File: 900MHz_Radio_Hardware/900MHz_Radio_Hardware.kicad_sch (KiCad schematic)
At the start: 27 parts, among them SW1 SW_SPDT, U1 TSR_1-2450

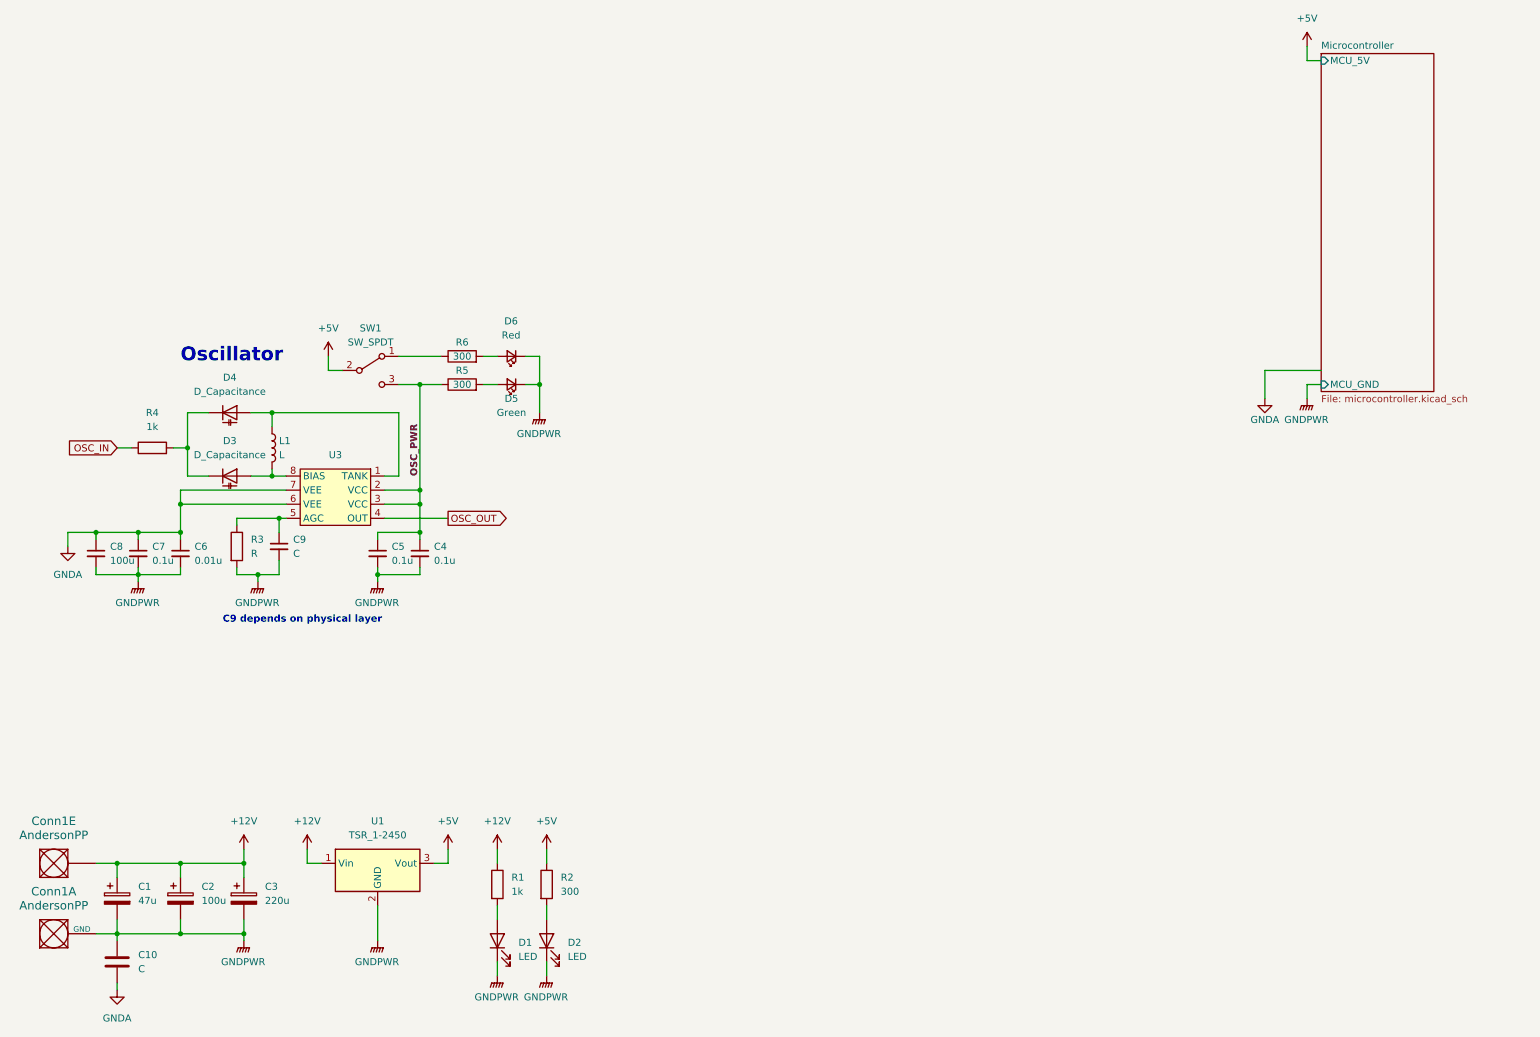
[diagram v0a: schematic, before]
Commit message: Worked on oscillator tank
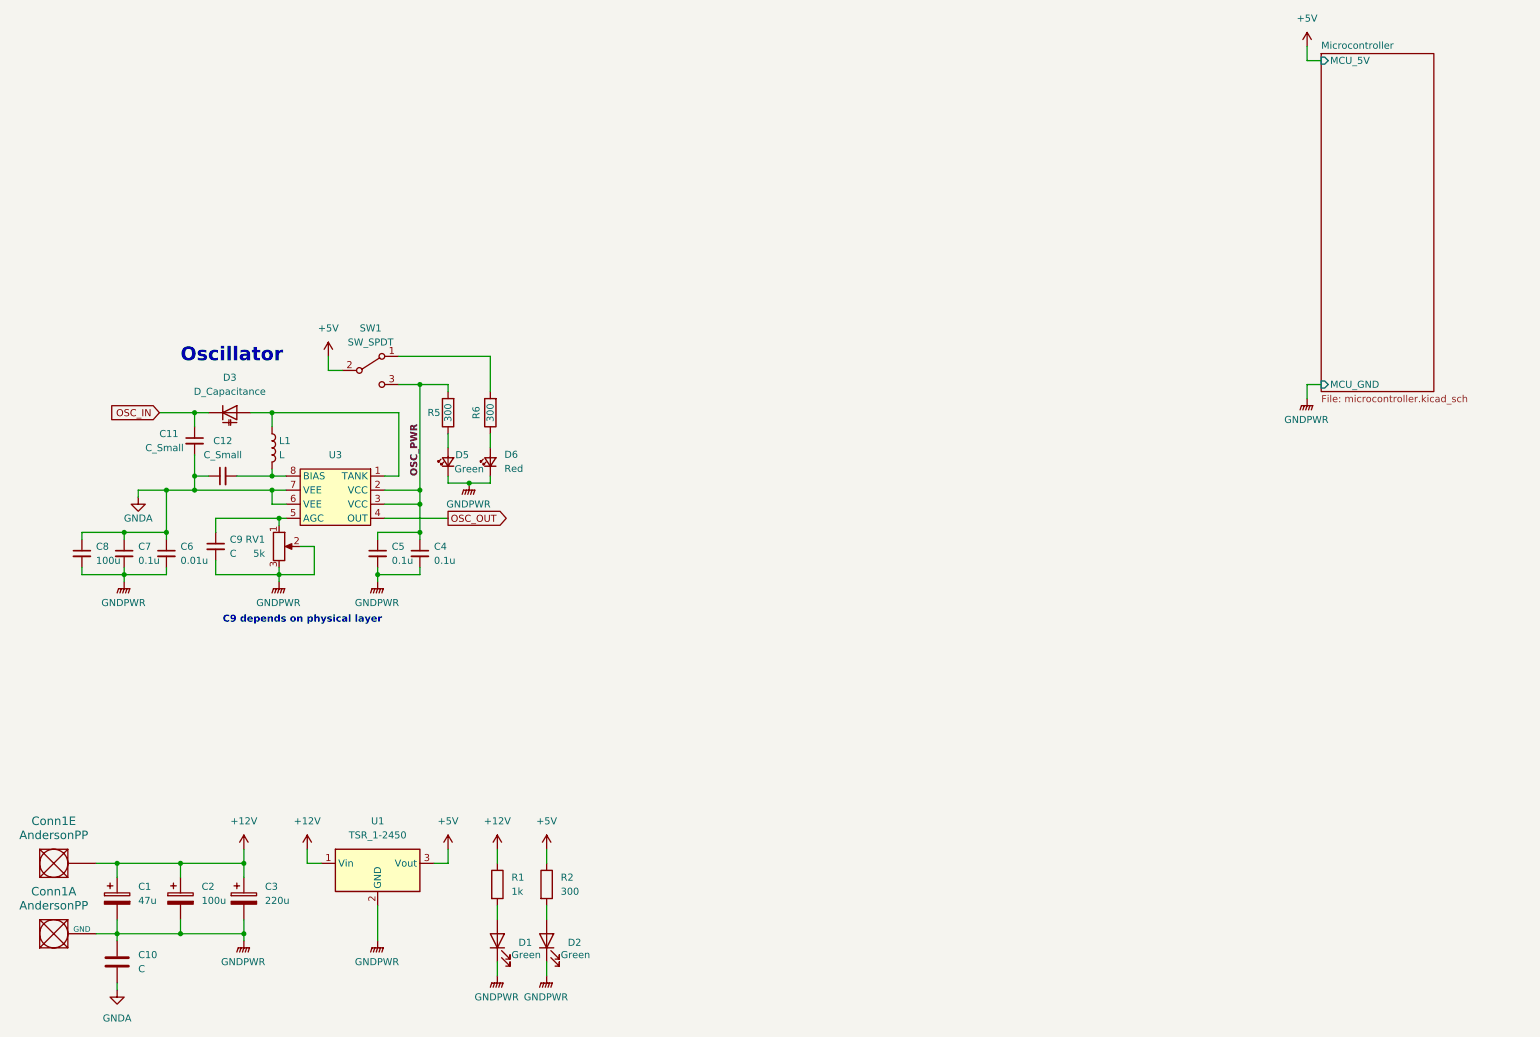
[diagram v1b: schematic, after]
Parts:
- removed D4: D_Capacitance, symbol Device:D_Capacitance
- removed R3: R, symbol Device:R
- removed R4: 1k, symbol Device:R
- added C11, C12: C_Small, symbol Device:C_Small
- added RV1: 5k, symbol Device:R_Potentiometer
- D1, D2: value LED -> Green
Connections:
- net GNDA: now also C11.2, C12.1
- net GNDPWR: now also RV1.2, RV1.3
- net OSC_IN: now also D3.1 (K), C11.1
- net OSC_PWR: now also R5.2; no longer R5.1
- net at L1.2, U3.8 (BIAS): now also C12.2; no longer D3.2 (A)
- net at D6.2 (A): now also R6.1; no longer R6.2
- net at L1.1, U3.1 (TANK): now also D3.2 (A)
- net at C9.1, U3.5 (AGC): now also RV1.1
- net at SW1.1 (A): now also R6.2; no longer R6.1
- net at D5.2 (A): now also R5.1; no longer R5.2
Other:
- moved on the sheet: C6, C7, C8, C9, D3, D5, D6, R5, R6

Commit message: Replaced oscillator
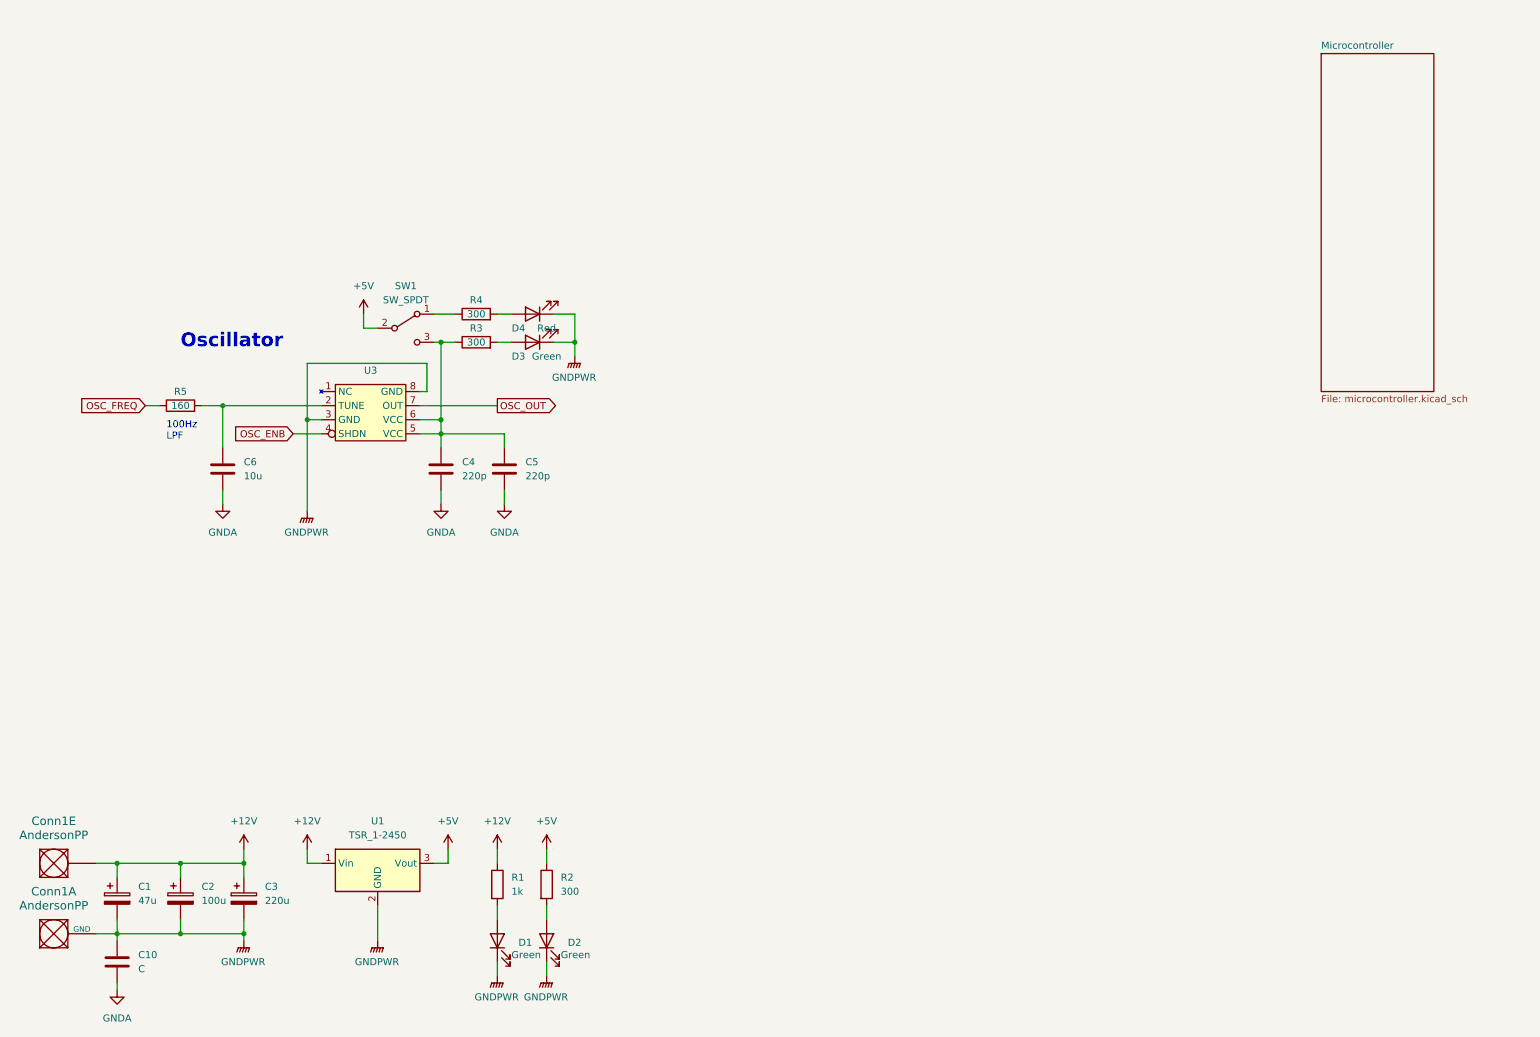
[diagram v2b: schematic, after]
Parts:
- removed C11, C12: C_Small, symbol Device:C_Small
- removed C4, C5, C7: 0.1u, symbol Device:C_Small
- removed C6: 0.01u, symbol Device:C_Small
- removed C8: 100u, symbol Device:C_Small
- removed C9: C, symbol Device:C_Small
- removed D3: D_Capacitance, symbol Device:D_Capacitance
- removed D5: Green, symbol Device:LED_Small
- removed D6: Red, symbol Device:LED_Small
- removed L1: L, symbol Device:L
- removed R6: 300, symbol Device:R
- removed RV1: 5k, symbol Device:R_Potentiometer
- removed U3: ~, Package_SO:SOIC-8_3.9x4.9mm_P1.27mm, symbol MRDT_ICs:MC100EL1648DG
- added C4, C5: 220p, symbol Device:C
- added C6: 10u, symbol Device:C
- added D3: Green, symbol Device:LED
- added D4: Red, symbol Device:LED
- added R3, R4: 300, symbol Device:R
- added U3: ~, Package_SO:MSOP-8_3x3mm_P0.65mm, symbol MRDT_ICs:MAX2623EUA+T
- R5: value 300 -> 160
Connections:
- net GNDA: now also C4.2, C5.2, C6.2
- net GNDPWR: now also D3.1 (K), D4.1 (K), U3.3 (GND), U3.8 (GND)
- net OSC_OUT: now also U3.7 (OUT)
- net at SW1.1 (A): now also R4.1
- net OSC_FREQ: now reaches R5.1
- net OSC_PWR: no longer names the net of SW1.3 (C)
- net OSC_PWR: now also C4.1, C5.1, R3.1, U3.5 (VCC), U3.6 (VCC); no longer R5.2
- new net: D3.2 (A), R3.2
- new net: C6.1, R5.2, U3.2 (TUNE)
- new net: D4.2 (A), R4.2
- new net OSC_ENB: U3.4 (SHDN)
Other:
- sheet Microcontroller ports: added none; removed MCU_5V, MCU_GND
- note added: "100Hz LPF"
- note removed: "C9 depends on physical layer"

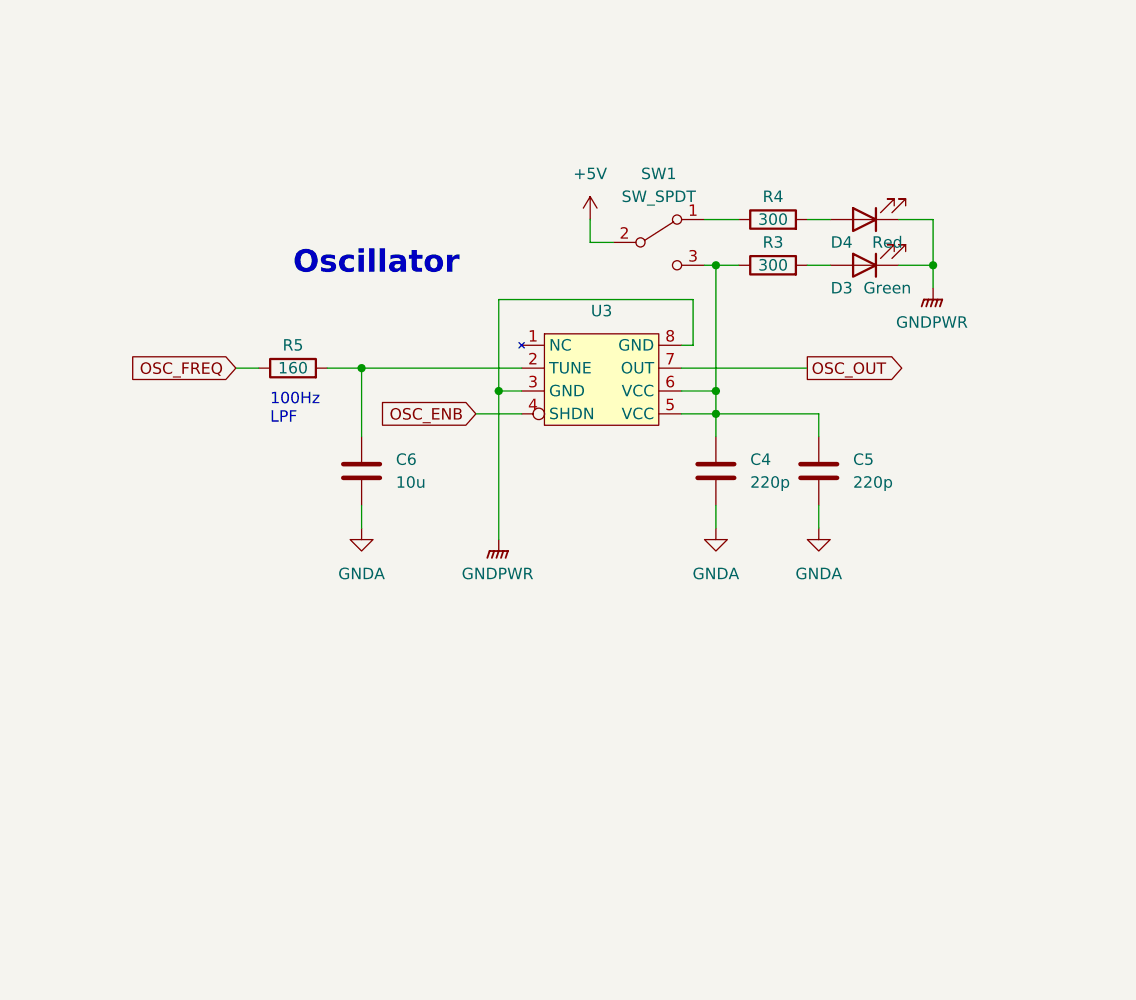
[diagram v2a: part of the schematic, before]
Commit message: Oscillator control circuit
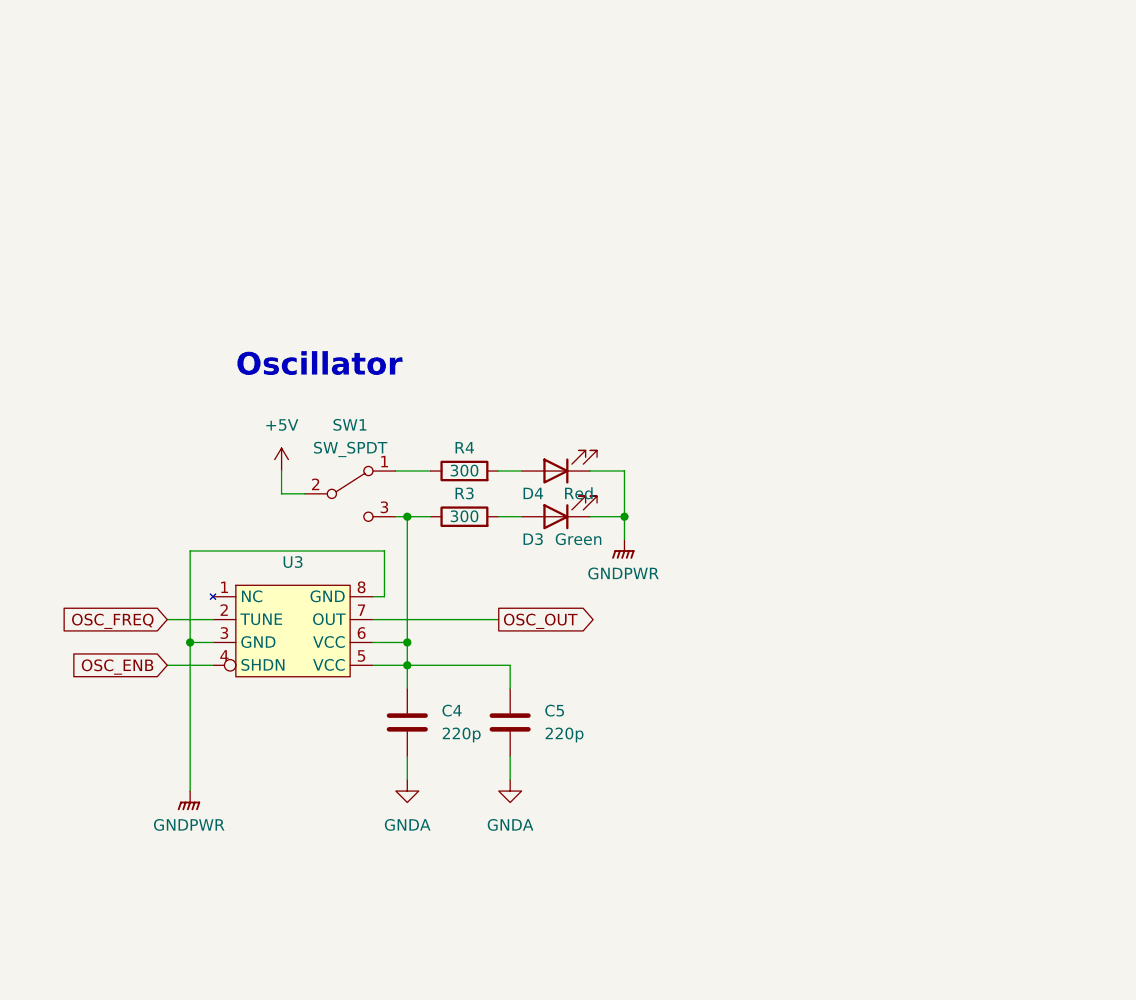
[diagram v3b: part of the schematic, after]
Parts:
- removed C6: 10u, symbol Device:C
- removed R5: 160, symbol Device:R
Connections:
- net OSC_FREQ: now also U3.2 (TUNE)
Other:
- note removed: "100Hz LPF"
- moved on the sheet: C4, C5, D3, D4, R3, R4, SW1, U3

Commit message: Updated filter
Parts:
- removed C4, C5: 220p, symbol Device:C
- removed D3: Green, symbol Device:LED
- removed D4: Red, symbol Device:LED
- removed R3, R4: 300, symbol Device:R
- removed SW1: SW_SPDT, symbol Switch:SW_SPDT
- removed U3: ~, Package_SO:MSOP-8_3x3mm_P0.65mm, symbol MRDT_ICs:MAX2623EUA+T
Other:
- added sheet Oscillator (oscillator.kicad_sch)
- note removed: "Oscillator"
